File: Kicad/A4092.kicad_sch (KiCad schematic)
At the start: 0 parts

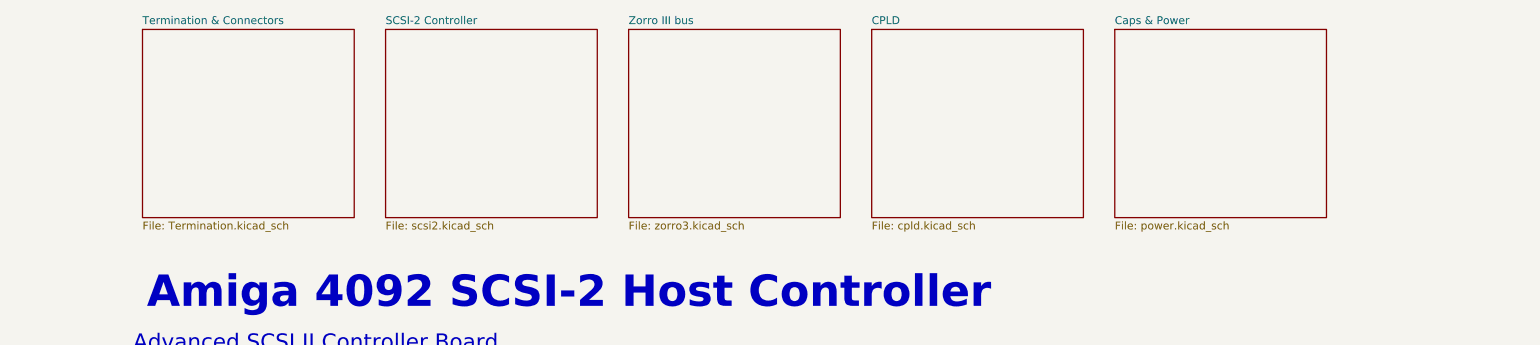
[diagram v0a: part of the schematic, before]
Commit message: Hook up Flash page
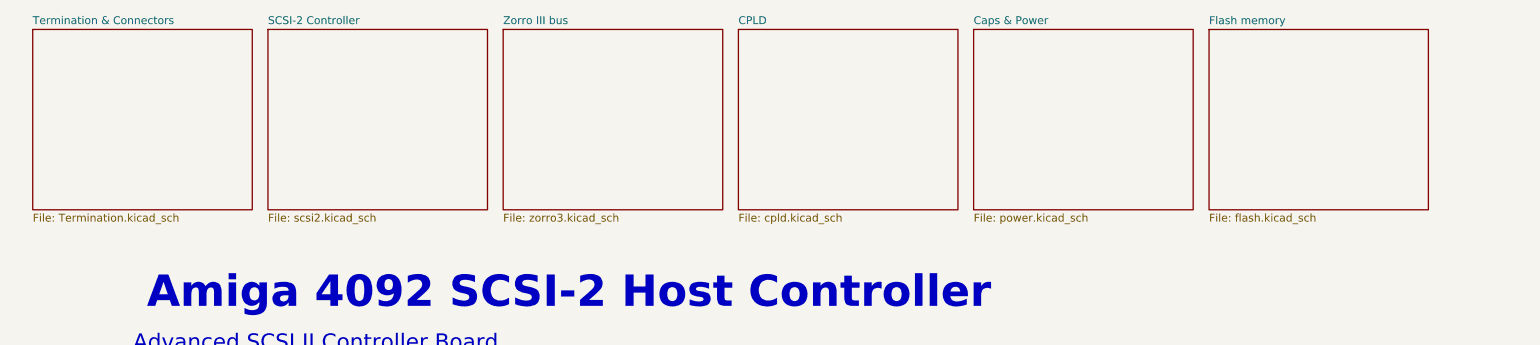
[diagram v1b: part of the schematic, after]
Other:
- added sheet Flash memory (flash.kicad_sch)
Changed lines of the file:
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@@
 	)
 	(sheet
-		(at 210.82 21.59)
-		(size 34.29 30.48)
+		(at 187.96 21.59)
+		(size 35.56 29.21)
 		(exclude_from_sim no)
 		(in_bom yes)
@@
 		)
 		(property "Sheetname" "Caps & Power"
-			(at 210.82 20.8784 0)
+			(at 187.96 20.8784 0)
 			(effects
 				(font
@@
 		)
 		(property "Sheetfile" "power.kicad_sch"
-			(at 210.82 52.6546 0)
+			(at 187.96 51.3846 0)
 			(effects
 				(font
@@
 	)
 	(sheet
-		(at 92.71 21.59)
-		(size 34.29 30.48)
+		(at 73.66 21.59)
+		(size 35.56 29.21)
 		(exclude_from_sim no)
 		(in_bom yes)
@@
 		)
 		(property "Sheetname" "SCSI-2 Controller"
-			(at 92.71 20.8784 0)
+			(at 73.66 20.8784 0)
 			(effects
 				(font
@@
 		)
 		(property "Sheetfile" "scsi2.kicad_sch"
-			(at 92.71 52.6546 0)
+			(at 73.66 51.3846 0)
 			(effects
 				(font
@@
 	)
 	(sheet
-		(at 53.34 21.59)
-		(size 34.29 30.48)
+		(at 35.56 21.59)
+		(size 35.56 29.21)
 		(exclude_from_sim no)
 		(in_bom yes)
@@
 		)
 		(property "Sheetname" "Termination & Connectors"
-			(at 53.34 20.8784 0)
+			(at 35.56 20.8784 0)
 			(effects
 				(font
@@
 		)
 		(property "Sheetfile" "Termination.kicad_sch"
-			(at 53.34 52.6546 0)
+			(at 35.56 51.3846 0)
 			(effects
 				(font
@@
 	)
 	(sheet
-		(at 132.08 21.59)
-		(size 34.29 30.48)
+		(at 111.76 21.59)
+		(size 35.56 29.21)
 		(exclude_from_sim no)
 		(in_bom yes)
@@
 		)
 		(property "Sheetname" "Zorro III bus"
-			(at 132.08 20.8784 0)
+			(at 111.76 20.8784 0)
 			(effects
 				(font
@@
 		)
 		(property "Sheetfile" "zorro3.kicad_sch"
-			(at 132.08 52.6546 0)
+			(at 111.76 51.3846 0)
 			(effects
 				(font
@@
 	)
 	(sheet
-		(at 171.45 21.59)
-		(size 34.29 30.48)
+		(at 226.0914 21.5967)
+		(size 35.5286 29.2033)
+		(exclude_from_sim no)
+		(in_bom yes)
+		(on_board yes)
+		(dnp no)
+		(fields_autoplaced yes)
+		(stroke
+			(width 0.1524)
+			(type solid)
+		)
+		(fill
+			(color 0 0 0 0.0000)
+		)
+		(property "Sheetname" "Flash memory"
+			(at 226.0914 20.8851 0)
+			(effects
+				(font
+					(size 1.27 1.27)
+				)
+				(justify left bottom)
+			)
+		)
+		(property "Sheetfile" "flash.kicad_sch"
+			(at 226.0914 51.3846 0)
+			(effects
+				(font
+					(size 1.27 1.27)
+				)
+				(justify left top)
+			)
+		)
+		(instances
+			(project "A4092"
+				(path "/8f9f4021-47aa-41d9-bea7-f6ccf72098bb"
+					(page "7")
+				)
+			)
+		)
+	)
+	(sheet
+		(at 149.86 21.59)
+		(size 35.56 29.21)
 		(exclude_from_sim no)
 		(in_bom yes)
@@
 		)
 		(property "Sheetname" "CPLD"
-			(at 171.45 20.8784 0)
+			(at 149.86 20.8784 0)
 			(effects
 				(font
@@
 		)
 		(property "Sheetfile" "cpld.kicad_sch"
-			(at 171.45 52.6546 0)
-			(effects
-				(font
+			(at 149.86 51.3846 0)
+			(effects
+				(font
